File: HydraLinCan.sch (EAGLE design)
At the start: 33 parts, among them CN1 8p-2.54, J1 HYDRABUS_SHIELD_CON_HEADER_2X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, J2 HYDRABUS_SHIELD_CON_HEADER_2X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, J3 HYDRABUS_SHIELD_CON_HEADER_2X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, K1 TS-1188E, U1 SN65HVD233DG4, U2 SN65HVD233DG4, U3 CJ78M05-to252

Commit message: 2 layers parts
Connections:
- net N$10 renamed CAN1_P
- net N$11 renamed CAN2_N
- net N$12 renamed CAN2_P
- net N$9 renamed CAN1_N

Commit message: Silkscreen cleaning
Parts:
- renumbered K1 to UBTN
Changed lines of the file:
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@@
 <part name="CAN1" library="jumper" deviceset="JP1E" device=""/>
 <part name="CAN2" library="jumper" deviceset="JP1E" device=""/>
-<part name="K1" library="Seeed-OPL-Button" deviceset="SMD-BUTTON-2+2P" device="" value="TS-1188E"/>
+<part name="UBTN" library="Seeed-OPL-Button" deviceset="SMD-BUTTON-2+2P" device="" value="TS-1188E"/>
 <part name="C1" library="Seeed-OPL-Capacitor" deviceset="CERAMIC-100NF-50V-20%-Y5V(0805)" device="" value="100NF"/>
 <part name="C2" library="Seeed-OPL-Capacitor" deviceset="CERAMIC-100NF-50V-20%-Y5V(0805)" device="" value="100NF"/>
@@
 <attribute name="VALUE" x="205.105" y="60.96" size="1.778" layer="96" rot="MR90"/>
 </instance>
-<instance part="K1" gate="K" x="49.53" y="51.308" smashed="yes" rot="R270">
+<instance part="UBTN" gate="K" x="49.53" y="51.308" smashed="yes" rot="R270">
 <attribute name="NAME" x="53.34" y="57.658" size="1.27" layer="95" ratio="10" rot="R270"/>
 <attribute name="VALUE" x="53.34" y="51.308" size="1.27" layer="96" ratio="10" rot="R270"/>
@@
 </segment>
 <segment>
-<pinref part="K1" gate="K" pin="1"/>
+<pinref part="UBTN" gate="K" pin="1"/>
 <wire x1="48.26" y1="57.658" x2="48.26" y2="62.484" width="0.1524" layer="91"/>
 <junction x="48.26" y="62.484"/>
@@
 <net name="N$21" class="0">
 <segment>
-<pinref part="K1" gate="K" pin="2"/>
+<pinref part="UBTN" gate="K" pin="2"/>
 <pinref part="R10" gate="G$1" pin="1"/>
 <wire x1="48.26" y1="44.958" x2="48.26" y2="37.846" width="0.1524" layer="91"/>

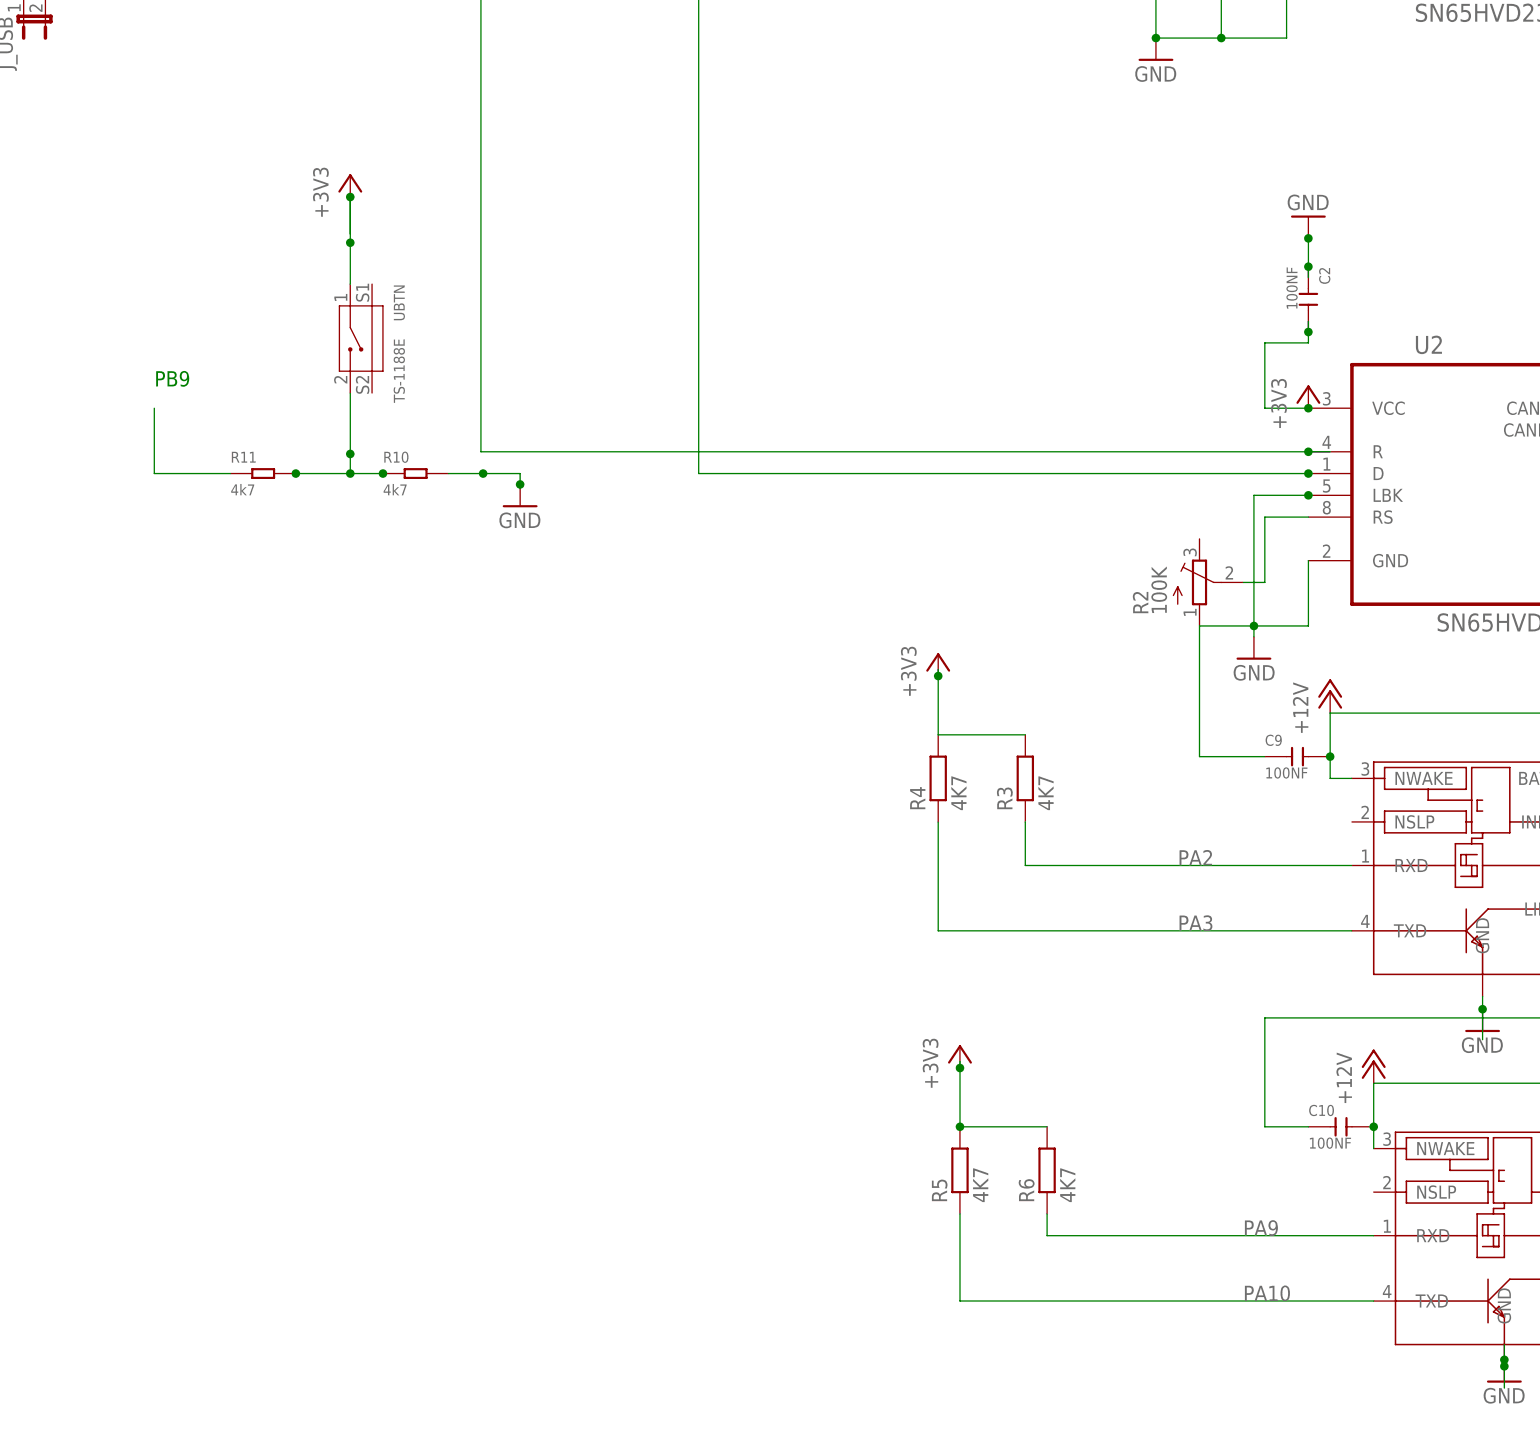
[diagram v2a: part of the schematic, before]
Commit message: Upgrade LIN transceivers for LIN2.0-2.2A/SAE J2602 and ISO 17984-4 compatibility
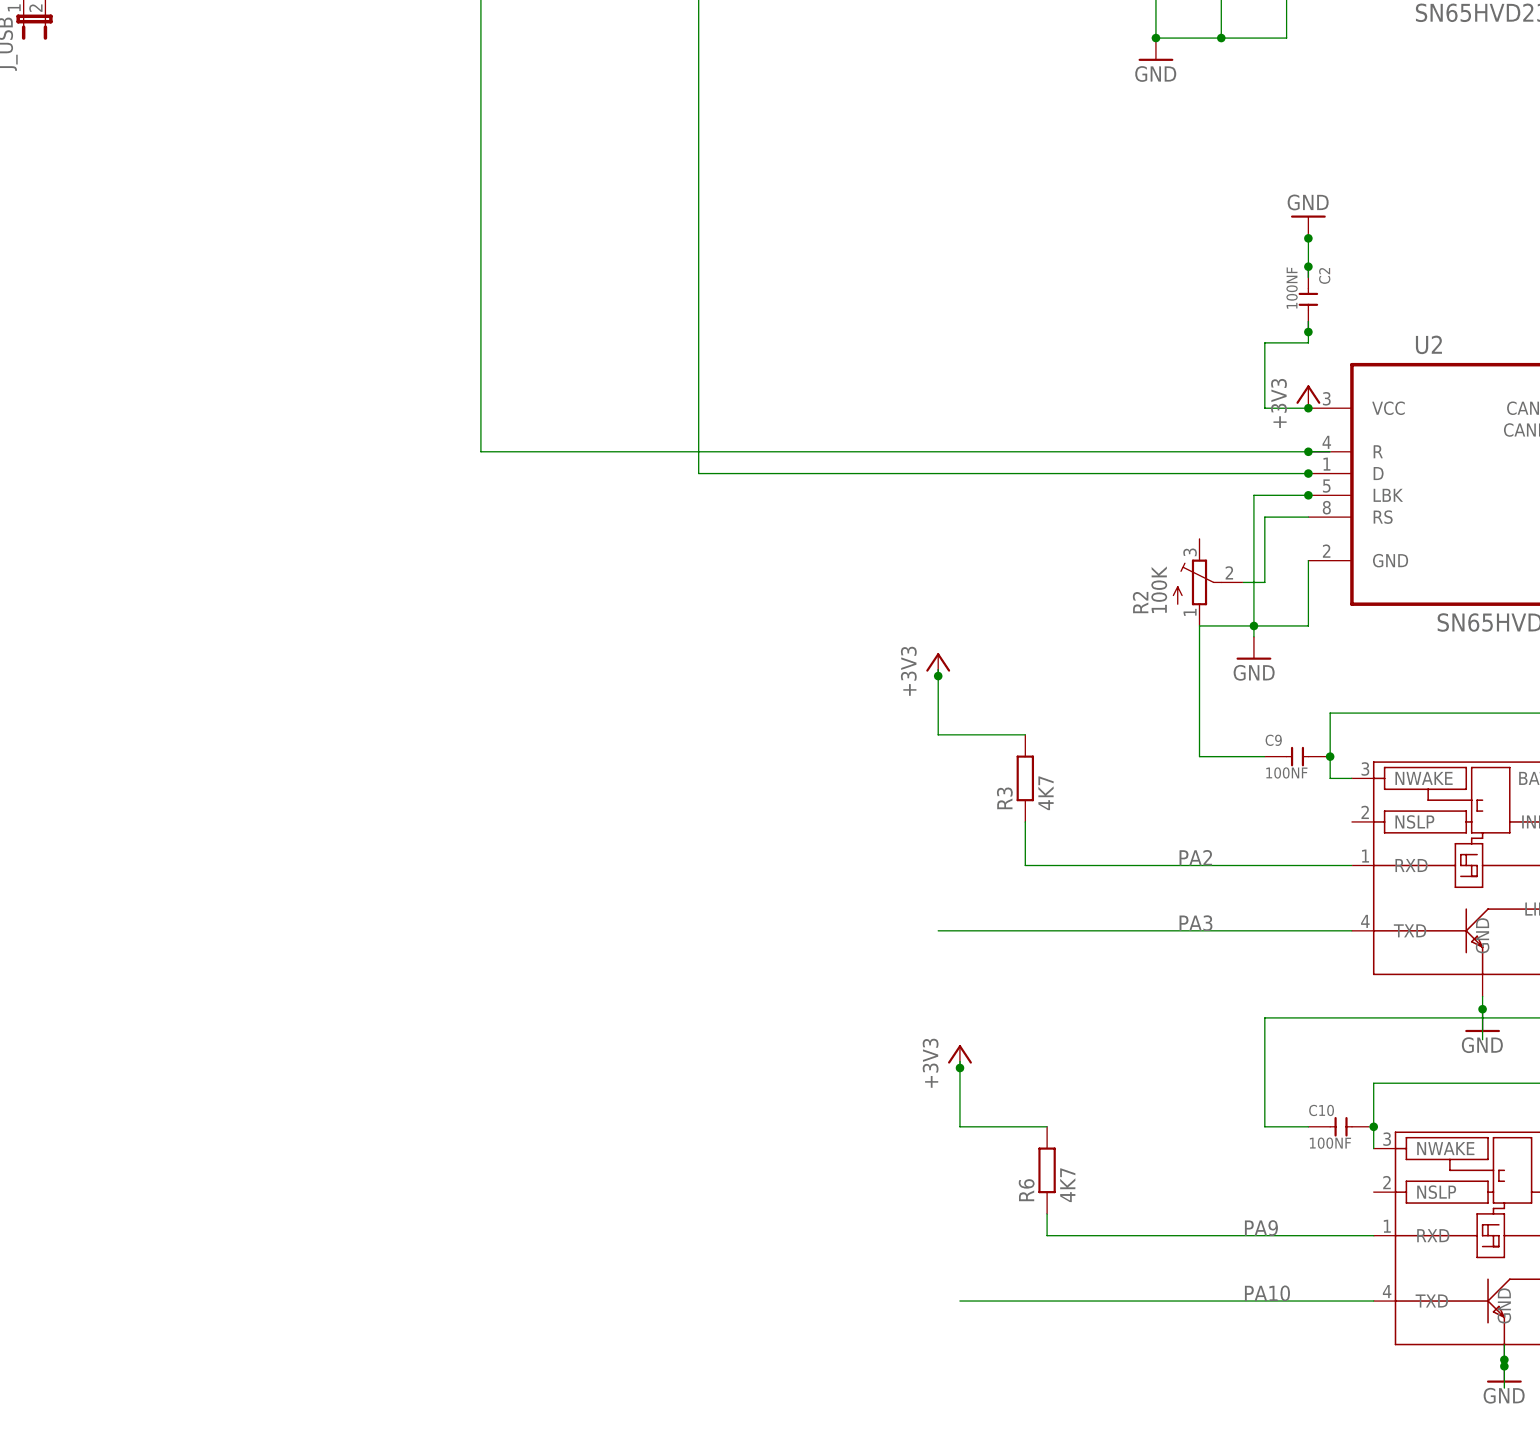
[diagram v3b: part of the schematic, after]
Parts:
- removed R10, R11: 4k7, Seeed-OPL-Resistor:SMD-RES-33K-1%-1/4W(1206)
- removed R4, R5: 4K7, resistor:R-EU_M1206
- removed UBTN: TS-1188E, Seeed-OPL-Button:SMD-BUTTON-2+2P
- LIN1, LIN2: value TJA1020SO8 -> TJA1021SO8
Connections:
- removed net N$21: R10.1, R11.2, UBTN.2
- new net N$10: C10.2, LIN2.INH, LIN2.NWAKE
- new net N$9: C9.2, LIN1.INH, LIN1.NWAKE
- net +12V: no longer C10.2, C9.2, LIN1.INH, LIN1.NWAKE, LIN2.INH, LIN2.NWAKE
- net +3V3: no longer R4.2, R5.2, UBTN.1
- net GND: no longer R10.2
- net PA10: no longer R5.1
- net PA3: no longer R4.1
- net PB7: no longer R11.1
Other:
- note removed: "PB9"
